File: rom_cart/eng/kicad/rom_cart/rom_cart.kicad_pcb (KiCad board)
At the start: 2 copper layers, 128.3 x 99.1 mm, 12 parts, among them J1 CONN_A2K6_CART_CARD, J2 CONN_512K_CART_CARD, SW1 SW_DIP_x04, SW2 SW_DIP_x04, U1 SST39SF040-70-4C-NHE, U2 74AHCT1G04

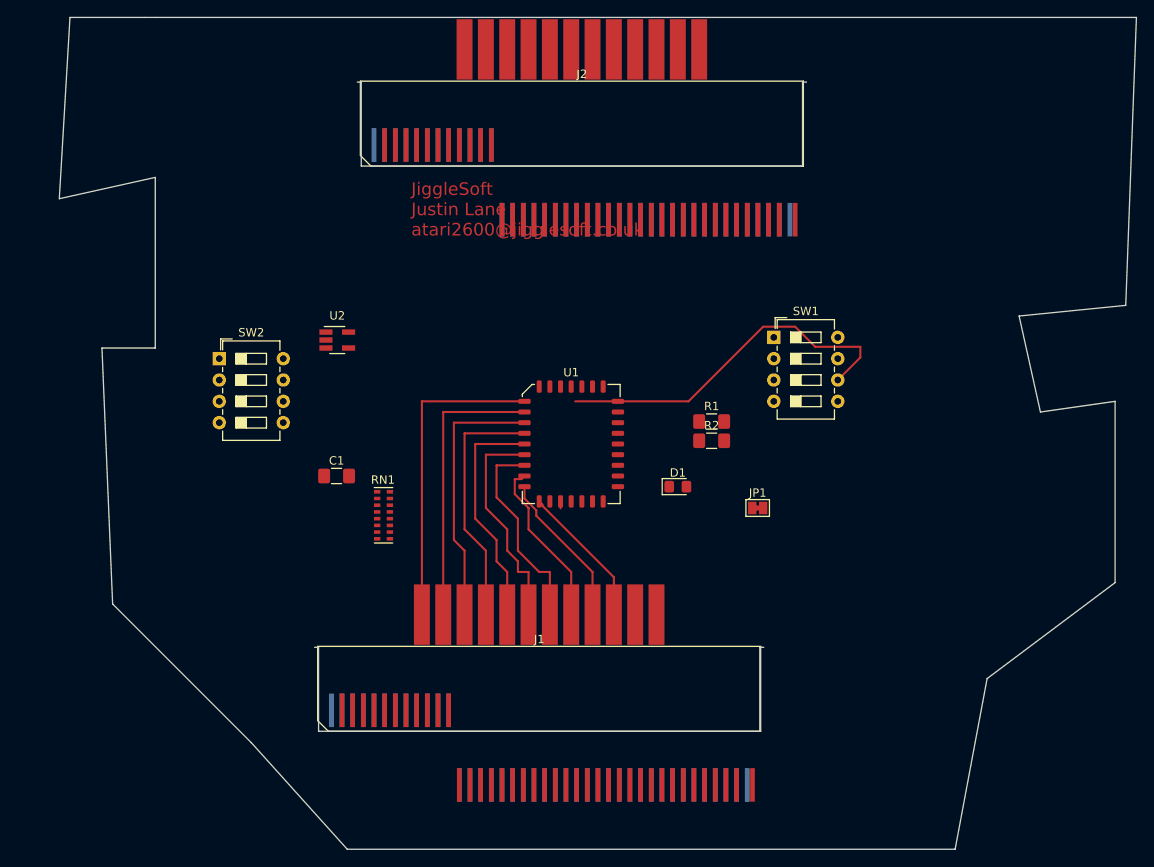
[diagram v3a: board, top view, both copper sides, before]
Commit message: Merge latest 'develop' branch into 'master' branch. (#1)
* Atari 2600 Budget Flash ROM Cartridge PCB layout Work-In-Progress.

* Added Cartridge Programmer Serial Protocol Doc (WIP).
Cartridge Programmer schematic (WIP).
ROM/RAM/PLD Cartridge project skeleton.

* New symbol libray for Microchip(Atmel) CPLD.
ROM/RAM/Bank Switching cartridge schematic (WIP).
Updated README.md file.

* Shared KiCAD libraries and modules migrated from atari2600_cart_prog repository develop branch to jigglesoft_kicad_library repository to be validated and sorted out.

* Added LICENCE.txt file to clarify licence in use.
Updated ROM cartridge schematic licence information.
Updated ROM cartridge schematic with current limiting resistor array to data bus.
Added initial document (WIP).
Updated cartridge programmer serial protocal document (WIP).

* Updated licence for cart_programmer schematic.
Updated licence for rom_ram_pld_cart schematic.
Updated component references from both of those schematics.
Latest cartridge programmer serial protocol checked in for backup (WIP).

* Updated .gitignore file (may need to remove .net files from repo).
Cartridge programmer schematic WIP.

* Added some pictures to README.md.
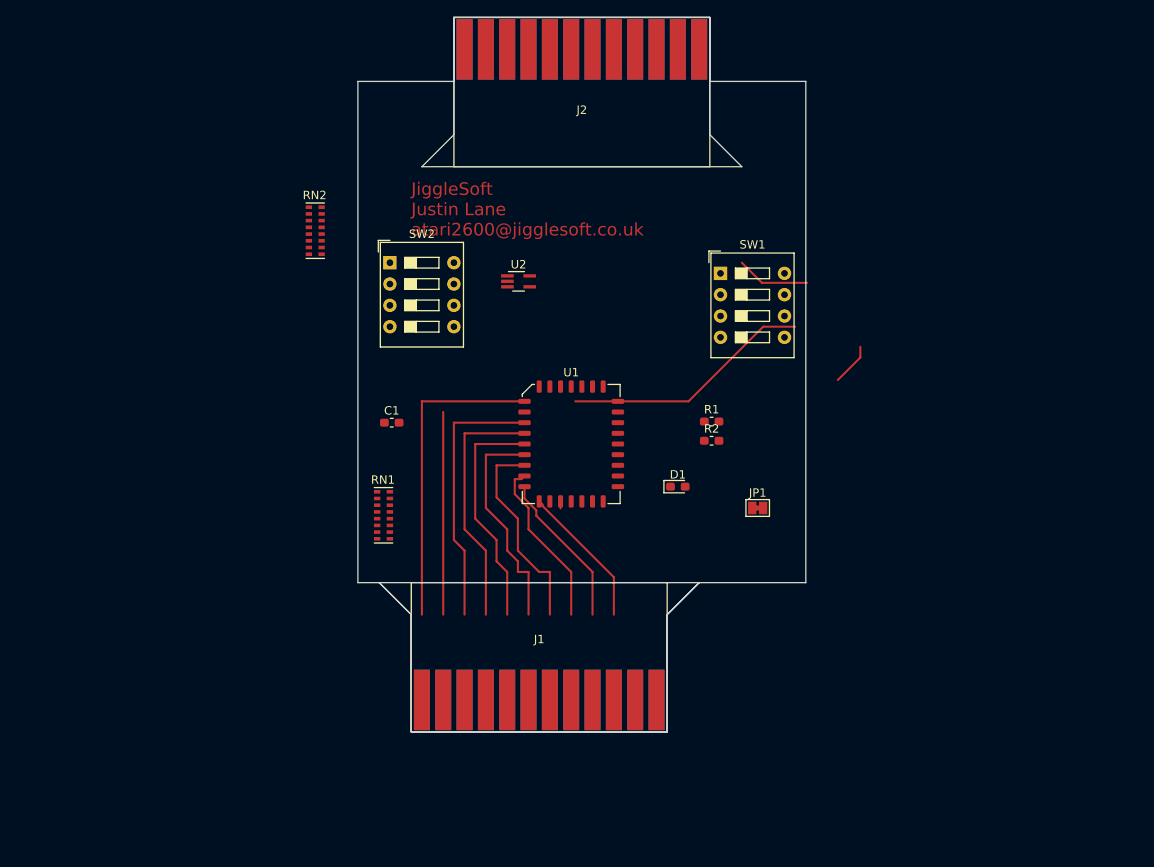
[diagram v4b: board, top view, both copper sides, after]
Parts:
- added RN2: R470 X 8, Resistor_SMD:R_Cat16-8, F.Cu at (116.8, 62.2)
- C1: footprint Capacitor_SMD:C_1206_3216Metric_Pad1.42x1.75mm_HandSolder -> Capacitor_SMD:C_0603_1608Metric_Pad1.05x0.95mm_HandSolder
- D1: footprint LED_SMD:LED_0805_2012Metric_Pad1.15x1.40mm_HandSolder -> LED_SMD:LED_0603_1608Metric_Pad1.05x0.95mm_HandSolder
- J1, J2: footprint JiggleSoft_Conn_Atari:Atari_2600_Cartridge_2x12_PCB_Edge -> Conn_Atari_JiggleSoft:Atari_2600_Cartridge_2x12_PCB_Edge
- R1, R2: footprint Resistor_SMD:R_1206_3216Metric_Pad1.42x1.75mm_HandSolder -> Resistor_SMD:R_0603_1608Metric_Pad1.05x0.95mm_HandSolder
- RN1: value R_Pack08 -> 10K X 8
- SW1, SW2: footprint Button_Switch_THT:SW_DIP_SPSTx04_Slide_6.7x11.72mm_W7.62mm_P2.54mm_LowProfile -> Button_Switch_THT:SW_DIP_SPSTx04_Slide_9.78x12.34mm_W7.62mm_P2.54mm
- U2: value 74AHCT1G04 -> 74HCT1G04; footprint Package_TO_SOT_SMD:SOT-23-5_HandSoldering -> Package_TO_SOT_SMD:SOT-353_SC-70-5_Handsoldering
- moved SW2 23.3 mm to (125.7, 66.0)
- moved U2 22.7 mm to (141.1, 68.3)
- moved SW1 9.92 mm to (165.1, 67.3)
- moved C1 9.14 mm to (125.9, 85.1)
- moved J2 7.62 mm to (148.6, 41.9), turned to 180 degrees
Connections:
- net /CS renamed /CE
- net Net-(U1-Pad22) renamed /~CE
- J2 pad 14: Net-(J2-Pad14) -> (no net)
- J2 pad 18: Net-(J2-Pad18) -> (no net)
- J2 pad 19: Net-(J2-Pad18) -> GND
- J2 pad 23: Net-(J2-Pad23) -> (no net)
- RN1 pad 1: Net-(RN1-Pad1) -> GND
- RN1 pad 2: Net-(RN1-Pad1) -> GND
- RN1 pad 3: Net-(RN1-Pad1) -> GND
- RN1 pad 4: Net-(RN1-Pad1) -> GND
- RN1 pad 5: Net-(RN1-Pad1) -> GND
- RN1 pad 6: Net-(RN1-Pad1) -> GND
- RN1 pad 7: Net-(RN1-Pad1) -> GND
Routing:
- net /A6: track 33.8 -> 24.1 mm
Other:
- board size 128.3 x 99.1 mm -> 53.3 x 85.1 mm

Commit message: Changed to through-hole caps and resistors. May back out.
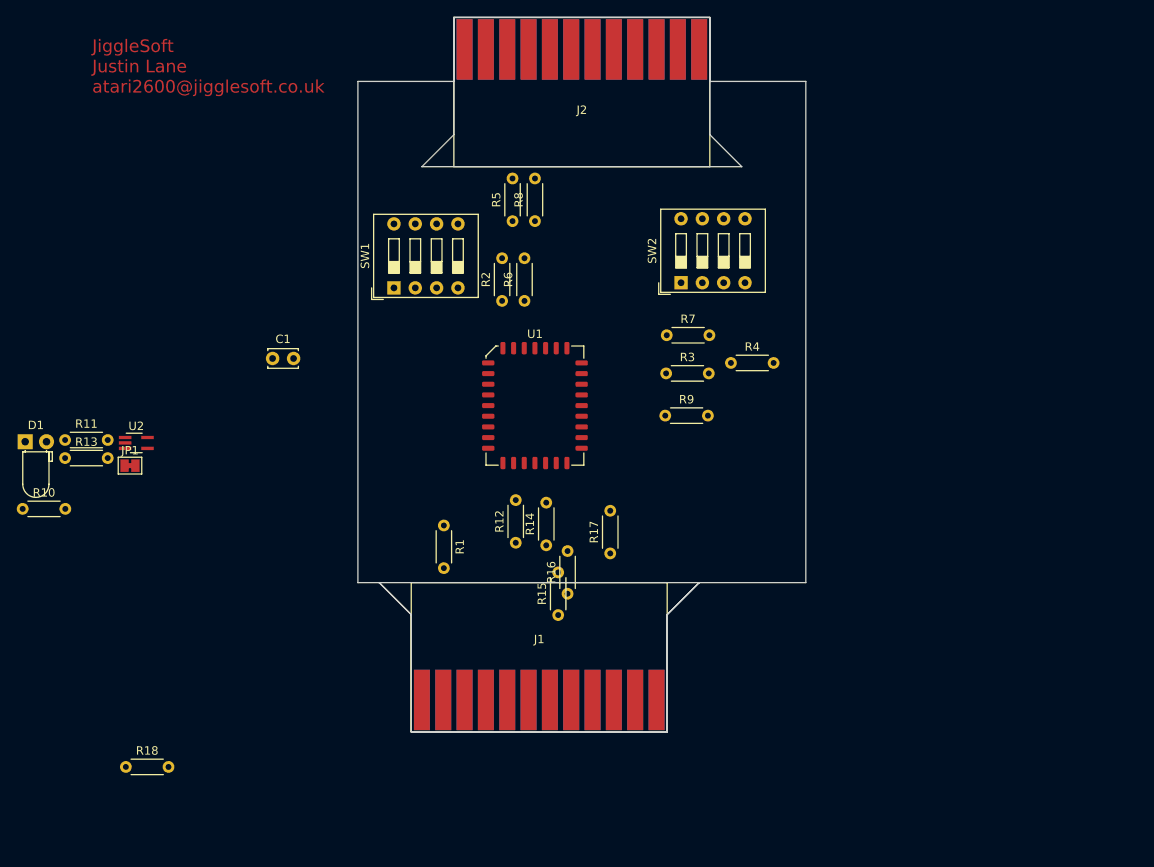
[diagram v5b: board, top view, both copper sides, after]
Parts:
- removed RN1: 10K X 8, Resistor_SMD:R_Cat16-8
- removed RN2: R470 X 8, Resistor_SMD:R_Cat16-8
- added R10: 470R, Resistor_THT:R_Axial_DIN0204_L3.6mm_D1.6mm_P5.08mm_Horizontal, F.Cu at (82.0, 95.4)
- added R11: 470R, Resistor_THT:R_Axial_DIN0204_L3.6mm_D1.6mm_P5.08mm_Horizontal, F.Cu at (87.0, 87.2)
- added R12: 470R, Resistor_THT:R_Axial_DIN0204_L3.6mm_D1.6mm_P5.08mm_Horizontal, F.Cu at (140.7, 99.4)
- added R13: 470R, Resistor_THT:R_Axial_DIN0204_L3.6mm_D1.6mm_P5.08mm_Horizontal, F.Cu at (87.0, 89.3)
- added R14: 470R, Resistor_THT:R_Axial_DIN0204_L3.6mm_D1.6mm_P5.08mm_Horizontal, F.Cu at (144.3, 99.7)
- added R15: 470R, Resistor_THT:R_Axial_DIN0204_L3.6mm_D1.6mm_P5.08mm_Horizontal, F.Cu at (145.8, 108.0)
- added R16: 470R, Resistor_THT:R_Axial_DIN0204_L3.6mm_D1.6mm_P5.08mm_Horizontal, F.Cu at (146.9, 105.5)
- added R17: 470R, Resistor_THT:R_Axial_DIN0204_L3.6mm_D1.6mm_P5.08mm_Horizontal, F.Cu at (152.0, 100.7)
- added R18: R, Resistor_THT:R_Axial_DIN0204_L3.6mm_D1.6mm_P5.08mm_Horizontal, F.Cu at (94.3, 126.1)
- added R3: 10K, Resistor_THT:R_Axial_DIN0204_L3.6mm_D1.6mm_P5.08mm_Horizontal, F.Cu at (158.6, 79.2)
- added R4: 10K, Resistor_THT:R_Axial_DIN0204_L3.6mm_D1.6mm_P5.08mm_Horizontal, F.Cu at (166.3, 78.0)
- added R5: 10K, Resistor_THT:R_Axial_DIN0204_L3.6mm_D1.6mm_P5.08mm_Horizontal, F.Cu at (140.3, 61.1)
- added R6: 10K, Resistor_THT:R_Axial_DIN0204_L3.6mm_D1.6mm_P5.08mm_Horizontal, F.Cu at (141.8, 70.6)
- added R7: 10K, Resistor_THT:R_Axial_DIN0204_L3.6mm_D1.6mm_P5.08mm_Horizontal, F.Cu at (158.7, 74.7)
- added R8: 10K, Resistor_THT:R_Axial_DIN0204_L3.6mm_D1.6mm_P5.08mm_Horizontal, F.Cu at (143.0, 61.1)
- added R9: 10K, Resistor_THT:R_Axial_DIN0204_L3.6mm_D1.6mm_P5.08mm_Horizontal, F.Cu at (158.5, 84.3)
- C1: footprint Capacitor_SMD:C_0603_1608Metric_Pad1.05x0.95mm_HandSolder -> Capacitor_THT:C_Disc_D3.4mm_W2.1mm_P2.50mm
- D1: footprint LED_SMD:LED_0603_1608Metric_Pad1.05x0.95mm_HandSolder -> LED_THT:LED_D3.0mm_Horizontal_O1.27mm_Z2.0mm_Clear
- R1: footprint Resistor_SMD:R_0603_1608Metric_Pad1.05x0.95mm_HandSolder -> Resistor_THT:R_Axial_DIN0204_L3.6mm_D1.6mm_P5.08mm_Horizontal
- R2: value R -> 10K; footprint Resistor_SMD:R_0603_1608Metric_Pad1.05x0.95mm_HandSolder -> Resistor_THT:R_Axial_DIN0204_L3.6mm_D1.6mm_P5.08mm_Horizontal
- moved D1 77.9 mm to (82.3, 87.4)
- moved JP1 74.9 mm to (94.8, 90.2)
- moved U2 49.4 mm to (95.5, 87.5)
- moved SW1 38.9 mm to (126.2, 69.0), turned to 90 degrees
- moved SW2 34.8 mm to (160.4, 68.4), turned to 90 degrees
- moved R1 34.2 mm to (132.2, 97.3), turned to 270 degrees
- moved R2 30.0 mm to (139.1, 70.6), turned to 90 degrees
- moved C1 16.1 mm to (111.8, 77.4)
- moved U1 6.29 mm to (143.0, 83.1)
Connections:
- R2 pad 1: Net-(JP1-Pad2) -> /A12
- R2 pad 2: Net-(D1-Pad2) -> GND
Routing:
- net /A14: track 43.7 -> 0.00 mm
- net /A7: track 37.6 -> 0.00 mm
- net /A5: track 31.8 -> 0.00 mm
- net /A4: track 30.1 -> 0.00 mm
- net /A3: track 27.8 -> 0.00 mm
- net /A2: track 26.5 -> 0.00 mm
- net /A1: track 24.5 -> 0.00 mm
- net /A6: track 24.1 -> 0.00 mm
- net /A0: track 20.2 -> 0.00 mm
- net /D0: track 18.6 -> 0.00 mm
- net /D1: track 17.2 -> 0.00 mm
- net GND: track 0.84 -> 0.00 mm
